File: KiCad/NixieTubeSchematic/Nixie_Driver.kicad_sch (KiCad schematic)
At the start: 24 parts

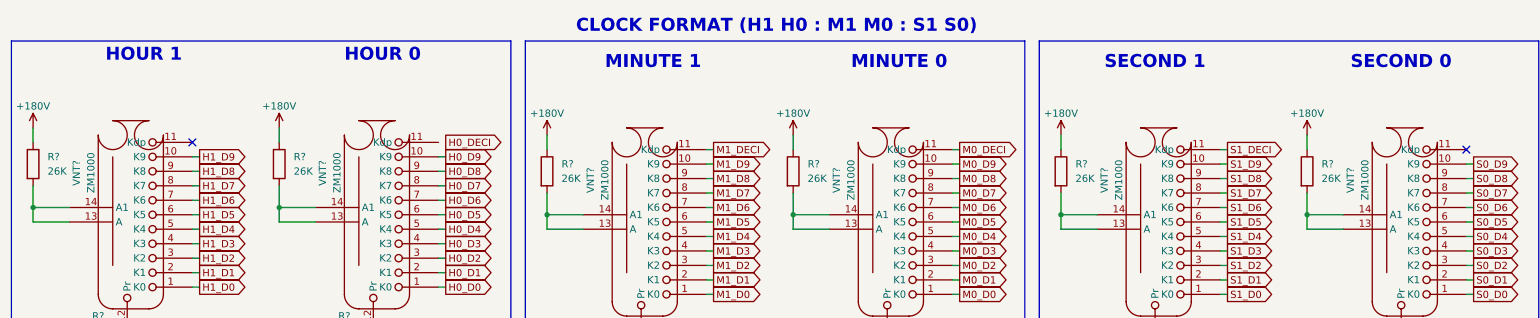
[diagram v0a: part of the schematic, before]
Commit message: Schematic for DS3231 RTC and AT24C32 EEPROM added
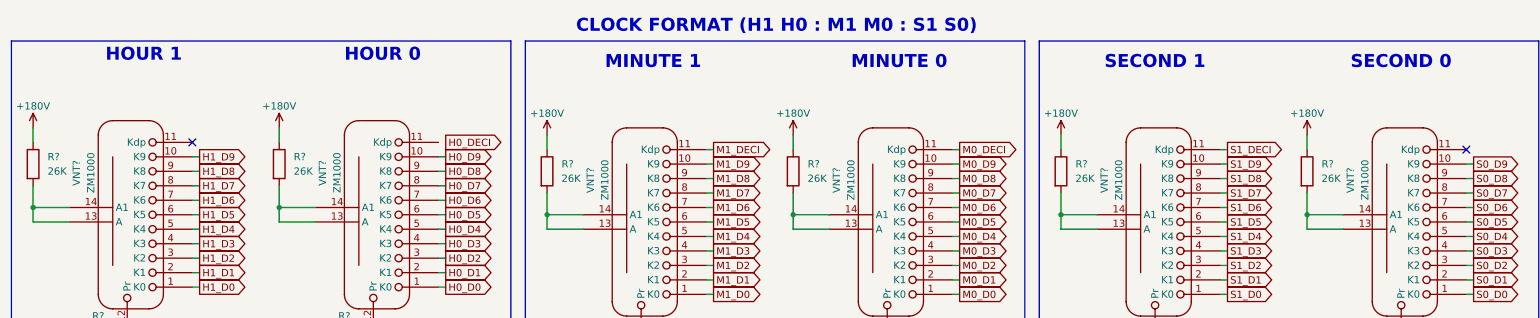
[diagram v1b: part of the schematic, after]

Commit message: Small changes
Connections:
- net BL_PIN: no longer U?.33 (*BL)
- net CLK_PIN: no longer U?.28 (CLK)
- net LE_PIN: no longer U?.31 (*LE)
- net DATA_IN renamed DATA_IN_HV
- new net BL_PIN_HV: U?.33 (*BL)
- new net CLK_PIN_HV: U?.28 (CLK)
- new net LE_PIN_HV: U?.31 (*LE)
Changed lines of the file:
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@@
     )
   )
-  (global_label "DATA_IN" (shape input) (at 67.31 133.35 180) (fields_autoplaced)
-    (effects (font (size 1.27 1.27)) (justify right))
-    (property "Intersheetrefs" "${INTERSHEET_REFS}" (at 57.5793 133.2706 0)
+  (global_label "DATA_IN_HV" (shape input) (at 67.31 133.35 180) (fields_autoplaced)
+    (effects (font (size 1.27 1.27)) (justify right))
+    (property "Intersheetrefs" "${INTERSHEET_REFS}" (at 53.6998 133.35 0)
       (effects (font (size 1.27 1.27)) (justify right) hide)
     )
@@
     )
   )
-  (global_label "BL_PIN" (shape input) (at 67.31 130.81 180) (fields_autoplaced)
-    (effects (font (size 1.27 1.27)) (justify right))
-    (property "Intersheetrefs" "${INTERSHEET_REFS}" (at 58.4259 130.7306 0)
+  (global_label "BL_PIN_HV" (shape input) (at 67.31 130.81 180) (fields_autoplaced)
+    (effects (font (size 1.27 1.27)) (justify right))
+    (property "Intersheetrefs" "${INTERSHEET_REFS}" (at 54.5465 130.81 0)
       (effects (font (size 1.27 1.27)) (justify right) hide)
     )
@@
     )
   )
-  (global_label "LE_PIN" (shape input) (at 67.31 135.89 180) (fields_autoplaced)
-    (effects (font (size 1.27 1.27)) (justify right))
-    (property "Intersheetrefs" "${INTERSHEET_REFS}" (at 58.5469 135.8106 0)
+  (global_label "LE_PIN_HV" (shape input) (at 67.31 135.89 180) (fields_autoplaced)
+    (effects (font (size 1.27 1.27)) (justify right))
+    (property "Intersheetrefs" "${INTERSHEET_REFS}" (at 54.6675 135.89 0)
       (effects (font (size 1.27 1.27)) (justify right) hide)
     )
@@
     )
   )
-  (global_label "CLK_PIN" (shape input) (at 67.31 143.51 180) (fields_autoplaced)
-    (effects (font (size 1.27 1.27)) (justify right))
-    (property "Intersheetrefs" "${INTERSHEET_REFS}" (at 57.1559 143.4306 0)
-      (effects (font (size 1.27 1.27)) (justify right) hide)
-    )
+  (global_label "CLK_PIN_HV" (shape input) (at 67.31 143.51 180) (fields_autoplaced)
+    (effects (font (size 1.27 1.27)) (justify right))
+    (property "Intersheetrefs" "${INTERSHEET_REFS}" (at 53.2765 143.51 0)
+      (effects (font (size 1.27 1.27)) (justify right) hide)
+    )
